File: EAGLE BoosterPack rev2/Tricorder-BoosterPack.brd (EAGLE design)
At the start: 63.9 x 44.2 mm, 39 parts, among them U1 MAG3110, U2 LMT70LMT70, U3 HDC1000, U4 OPT3001, U5 LMP91000, U6 PGA900

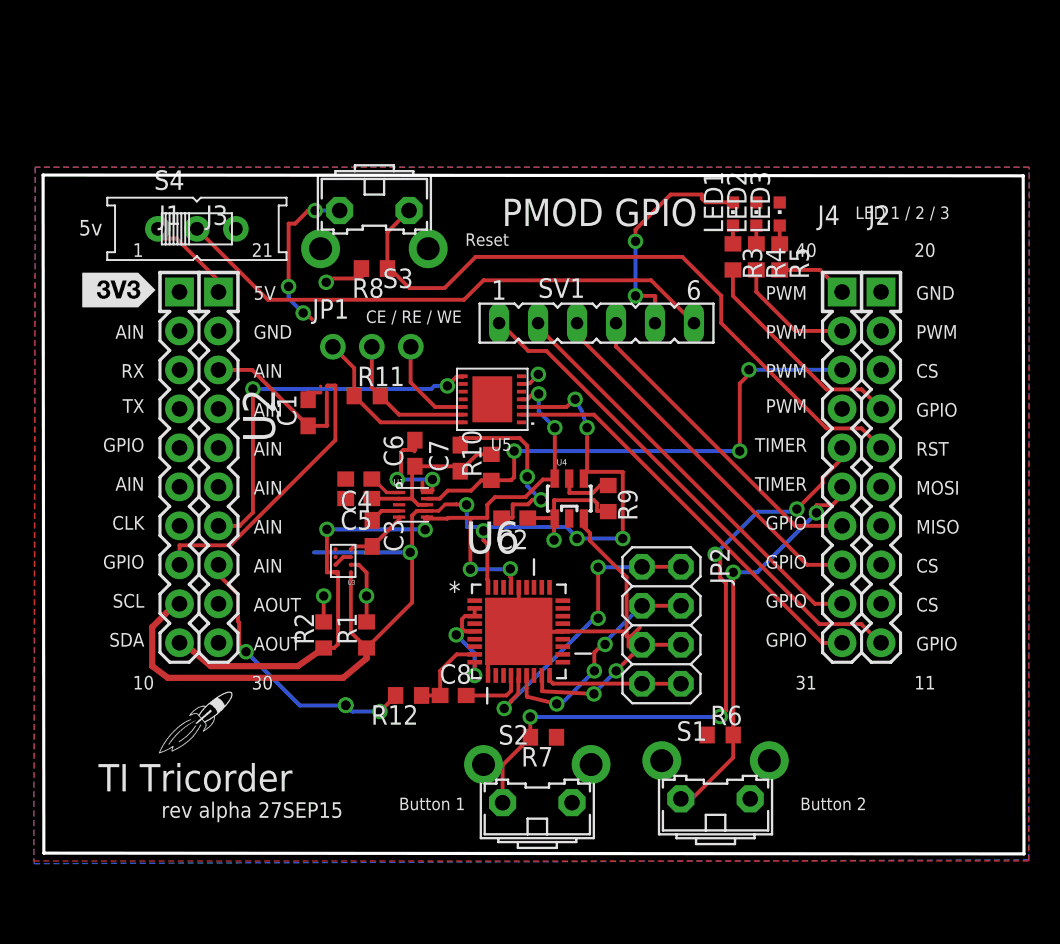
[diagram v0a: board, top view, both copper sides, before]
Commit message: Completed PGA900 circuit, add microSD card reader
Completed PGA900 circuit, add microSD card reader
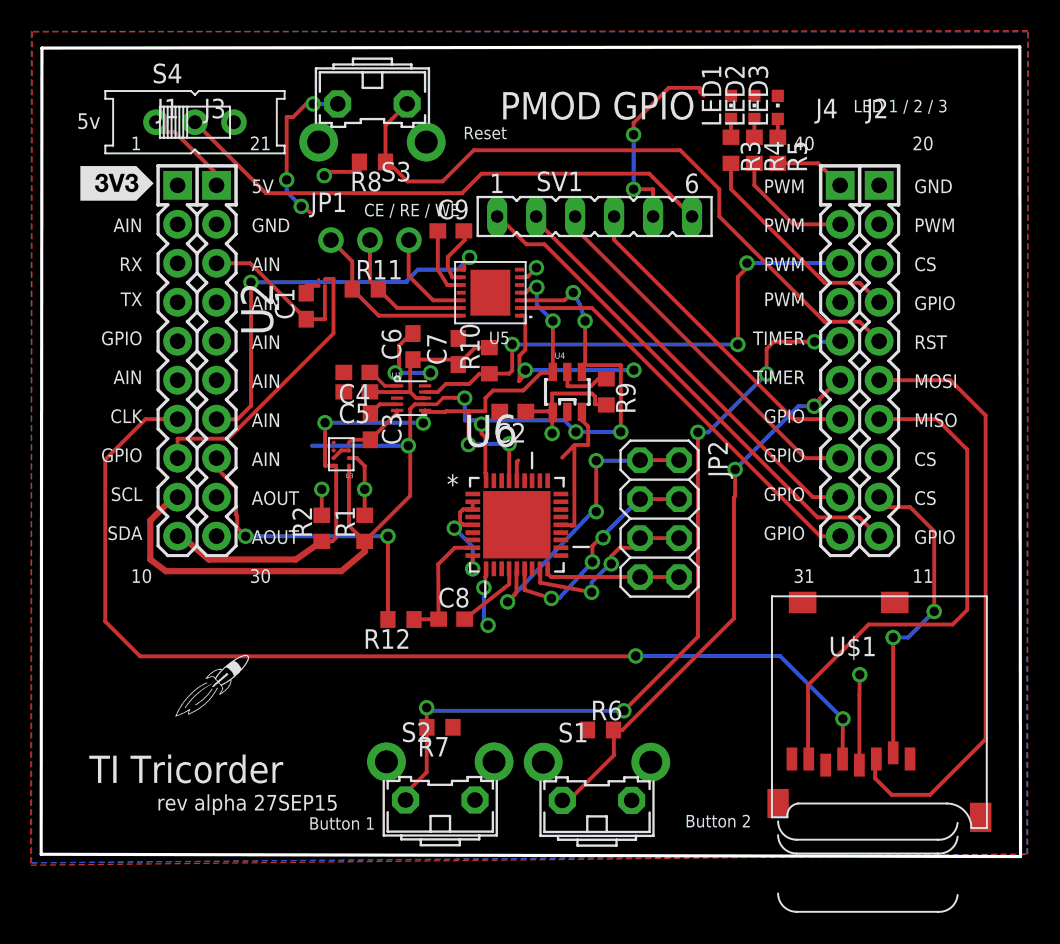
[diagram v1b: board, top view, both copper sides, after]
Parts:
- added C9: 0, adafruit:C0603
- added U$1: MICROSD, adafruit:MICROSD
- moved R6 7.81 mm to (37.9, 8.40)
- moved S1 7.73 mm to (37.7, 5.06)
- moved C6 6.95 mm to (25.7, 33.4)
- moved JP1 6.95 mm to (22.9, 40.3)
- moved LED1 6.95 mm to (46.4, 49.0)
- moved LED2 6.95 mm to (48.0, 49.0)
- moved LED3 6.95 mm to (49.5, 49.0)
- moved R10 6.95 mm to (30.7, 32.5)
- moved S3 6.95 mm to (23.1, 48.0)
- moved S4 6.95 mm to (11.5, 48.0)
- moved SV1 6.95 mm to (37.5, 41.9)
- moved U2 6.95 mm to (19.8, 37.5)
- moved JP2 6.95 mm to (41.8, 22.2)
- moved A1 6.95 mm to (10.4, 33.7)
- moved C1 6.95 mm to (18.7, 36.0)
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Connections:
- new net N$13: C9.2, U5.9
- new net N$7: C9.1, U5.10
- net 3V: now also U$1.4
- net GND: now also U$1.6, U$1.CD1, U$1.CD2, U$1.MT1, U$1.MT2
- net MISO: now also U$1.7
- net MOSI: now also U$1.3
- net SCLK: now also U$1.5
- net SD_CS: now also U$1.2
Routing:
- net SCLK: track 0.00 -> 69.7 mm, vias 0 -> 2
- net MOSI: track 0.00 -> 39.4 mm
- net MISO: track 0.00 -> 34.3 mm
- net SD_CS: track 0.00 -> 21.0 mm, vias 0 -> 2
- net GND: track 77.8 -> 65.3 mm, vias 9 -> 11
- net BTN1: track 41.5 -> 52.5 mm, vias 4 -> 5
- net BTN0: track 26.6 -> 36.2 mm
- net 3V: track 27.2 -> 33.1 mm, vias 7 -> 8
- net N$7: track 0.00 -> 4.60 mm
- net N$13: track 0.00 -> 4.28 mm
- net N$12: track 5.50 -> 7.88 mm
- net PGA900_VOUT: track 18.5 -> 20.6 mm, vias 4 -> 2
- net LMP91000_VOUT: track 24.7 -> 26.8 mm
- net N$10: track 4.06 -> 4.69 mm
- net VINPN: track 12.0 -> 12.5 mm
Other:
- board size 63.9 x 44.2 mm -> 63.8 x 52.8 mm

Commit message: Hardware Design Lock
Short of finding any showstopper bugs, the hardware design and BOM is
locked.
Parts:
- C1: value (none) -> 0
- moved C5 2.83 mm to (22.3, 33.2), turned to 90 degrees
- moved C6 1.95 mm to (23.8, 33.3)
- moved U$2 1.43 mm to (13.8, 10.5)
- moved C4 1.31 mm to (21.1, 30.8)
- moved C3 1.27 mm to (22.4, 29.3), turned to 180 degrees
- renumbered U$1 to U7
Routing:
- net GND: track 65.3 -> 102.8 mm, vias 11 -> 17
- net SCL: track 78.4 -> 71.5 mm, vias 7 -> 6
- net PGA900_VOUT: track 20.6 -> 17.9 mm
- net N$11: track 11.5 -> 12.7 mm
- net N$9: track 2.14 -> 2.73 mm
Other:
- board text added: "LED 1/2/PWR"
- board text removed: "LED 1 / 2 / 3"

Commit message: MAG3110 Circuit Fix
Removed R10, renumbered components
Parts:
- removed R12: 10k, resistor:R0603
- R10: value 10k -> 0
- R11: value 0 -> 10k
- moved R11 21.7 mm to (24.9, 15.6), turned to 180 degrees
- moved R10 9.33 mm to (22.6, 37.1), turned to 0 degrees
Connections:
- removed net N$11: C5.1, C6.1, C7.1, R10.2, U1.2, U1.8
- net 3V: now also C5.1, C6.1, C7.1, U1.2, U1.8
- net CE: now also R10.1; no longer R11.1
- net MAG_INT: no longer R10.1
- net N$12: now also R11.1; no longer R12.1
- net PGA900_VOUT: now also R11.2; no longer R12.2
- net RE: now also R10.2; no longer R11.2
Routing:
- net 3V: track 33.1 -> 46.0 mm, vias 8 -> 9
- net N$11: track 12.7 -> 0.00 mm
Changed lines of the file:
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@@
 <element name="C6" library="adafruit" package="C0603" value="1u" x="23.755" y="33.286" rot="R90"/>
 <element name="C7" library="adafruit" package="C0603" value="100n" x="28.657" y="33.065" rot="R90"/>
-<element name="R10" library="resistor" package="R0603" value="10k" x="30.685" y="32.465" rot="R90"/>
 <element name="U5" library="LMP91000" package="WFDFN-14" value="LMP91000" x="30.75" y="36.9" rot="R90">
 <attribute name="DIGIKEY" value="LMP91000SDE/NOPBCT-ND" x="30.75" y="36.9" size="1.778" layer="27" rot="R90" display="off"/>
 </element>
 <element name="JP1" library="adafruit" package="1X03-CLEANBIG" value="" x="22.9" y="40.325"/>
-<element name="R11" library="resistor" package="R0603" value="0" x="22.6" y="37.125"/>
+<element name="R10" library="resistor" package="R0603" value="0" x="22.6" y="37.125"/>
 <element name="U6" library="PGA900" package="QFN50P600X600X90-37N" value="PGA900" x="32.475" y="21.775">
 <attribute name="PACKAGE" value="QFN-36" x="32.475" y="21.775" size="1.778" layer="27" display="off"/>
@@
 </element>
 <element name="C8" library="adafruit" package="C0603" value="100n" x="28.225" y="15.625"/>
-<element name="R12" library="resistor" package="R0603" value="10k" x="24.925" y="15.6" rot="R180"/>
+<element name="R11" library="resistor" package="R0603" value="10k" x="24.925" y="15.6" rot="R180"/>
 <element name="JP2" library="adafruit" package="2X04" value="" x="41.775" y="22.175" rot="R270"/>
 <element name="C9" library="adafruit" package="C0603" value="0" x="28.175" y="40.925"/>
@@
 <wire x1="54.825" y1="12" x2="54.8" y2="10.65" width="0.254" layer="1"/>
 <via x="54.825" y="12" extent="1-16" drill="0.6096"/>
+<contactref element="U1" pad="8"/>
+<contactref element="C7" pad="1"/>
+<contactref element="C5" pad="1"/>
+<contactref element="C6" pad="1"/>
+<contactref element="U1" pad="2"/>
+<wire x1="22.317" y1="32.399" x2="22.354" y2="32.436" width="0.254" layer="1"/>
+<wire x1="22.354" y1="32.436" x2="23.755" y2="32.436" width="0.254" layer="1"/>
+<wire x1="26.494" y1="30.025" x2="25.8" y2="30.025" width="0.254" layer="1"/>
+<wire x1="25.8" y1="30.025" x2="25.4" y2="30.425" width="0.254" layer="1"/>
+<wire x1="25.4" y1="30.425" x2="24.674" y2="30.425" width="0.254" layer="1"/>
+<wire x1="23.755" y1="32.436" x2="23.966" y2="32.225" width="0.254" layer="1"/>
+<wire x1="23.966" y1="32.225" x2="25.075" y2="32.225" width="0.254" layer="1"/>
+<wire x1="25.075" y1="32.225" x2="25.45" y2="32.2" width="0.254" layer="1"/>
+<wire x1="25.45" y1="32.2" x2="25.4" y2="30.425" width="0.254" layer="1"/>
+<wire x1="28.657" y1="32.215" x2="28.192" y2="32.2" width="0.254" layer="1"/>
+<wire x1="28.192" y1="32.2" x2="26.275" y2="32.2" width="0.254" layer="1"/>
+<wire x1="26.275" y1="32.2" x2="25.45" y2="32.2" width="0.254" layer="1"/>
+<wire x1="26.275" y1="32.2" x2="26.275" y2="34.55" width="0.254" layer="1"/>
+<wire x1="26.275" y1="34.55" x2="26.275" y2="34.9" width="0.254" layer="1"/>
+<via x="26.275" y="34.55" extent="1-16" drill="0.6096"/>
 </signal>
 <signal name="DC">
@@
 <contactref element="A1" pad="38"/>
 <contactref element="U1" pad="9"/>
-<contactref element="R10" pad="1"/>
 <wire x1="46.875" y1="33.525" x2="46.875" y2="37.925" width="0.254" layer="1"/>
 <wire x1="32.175" y1="33.525" x2="46.875" y2="33.525" width="0.254" layer="16"/>
 <wire x1="32.175" y1="31.825" x2="32.175" y2="33.525" width="0.254" layer="1"/>
 <wire x1="31.975" y1="31.625" x2="32.175" y2="31.825" width="0.254" layer="1"/>
-<wire x1="30.775" y1="31.625" x2="31.975" y2="31.625" width="0.254" layer="1"/>
-<wire x1="30.775" y1="31.625" x2="30.685" y2="31.615" width="0.254" layer="1"/>
 <wire x1="47.475" y1="38.525" x2="46.875" y2="37.925" width="0.254" layer="1"/>
 <wire x1="47.475" y1="38.825" x2="47.475" y2="38.525" width="0.254" layer="1"/>
@@
 <wire x1="26.494" y1="30.425" x2="28.475" y2="30.425" width="0.254" layer="1"/>
 <wire x1="28.475" y1="30.425" x2="29.625" y2="31.225" width="0.254" layer="1"/>
-<wire x1="29.625" y1="31.225" x2="29.625" y2="31.6" width="0.254" layer="1"/>
-<wire x1="29.625" y1="31.6" x2="30.04" y2="31.615" width="0.254" layer="1"/>
-<wire x1="30.04" y1="31.615" x2="30.685" y2="31.615" width="0.254" layer="1"/>
+<wire x1="30.075" y1="31.575" x2="29.75" y2="31.25" width="0.254" layer="1"/>
+<wire x1="31.85" y1="31.575" x2="30.075" y2="31.575" width="0.254" layer="1"/>
+<wire x1="29.75" y1="31.25" x2="29.625" y2="31.225" width="0.254" layer="1"/>
+<wire x1="31.85" y1="31.575" x2="31.975" y2="31.625" width="0.254" layer="1"/>
 </signal>
 <signal name="LED1">
@@
 <wire x1="21.971" y1="30.825" x2="21.949" y2="30.803" width="0.254" layer="1"/>
 </signal>
-<signal name="N$11">
-<contactref element="U1" pad="8"/>
-<contactref element="C7" pad="1"/>
-<contactref element="C5" pad="1"/>
-<contactref element="C6" pad="1"/>
-<contactref element="R10" pad="2"/>
-<contactref element="U1" pad="2"/>
-<wire x1="30.675" y1="33.325" x2="30.685" y2="33.315" width="0.254" layer="1"/>
-<wire x1="30.675" y1="33.325" x2="29.565" y2="32.215" width="0.254" layer="1"/>
-<wire x1="29.565" y1="32.215" x2="28.657" y2="32.215" width="0.254" layer="1"/>
-<wire x1="22.317" y1="32.399" x2="22.354" y2="32.436" width="0.254" layer="1"/>
-<wire x1="22.354" y1="32.436" x2="23.755" y2="32.436" width="0.254" layer="1"/>
-<wire x1="26.494" y1="30.025" x2="25.8" y2="30.025" width="0.254" layer="1"/>
-<wire x1="25.8" y1="30.025" x2="25.4" y2="30.425" width="0.254" layer="1"/>
-<wire x1="25.4" y1="30.425" x2="24.674" y2="30.425" width="0.254" layer="1"/>
-<wire x1="23.755" y1="32.436" x2="23.966" y2="32.225" width="0.254" layer="1"/>
-<wire x1="23.966" y1="32.225" x2="25.075" y2="32.225" width="0.254" layer="1"/>
-<wire x1="25.075" y1="32.225" x2="25.45" y2="32.2" width="0.254" layer="1"/>
-<wire x1="25.45" y1="32.2" x2="25.4" y2="30.425" width="0.254" layer="1"/>
-<wire x1="28.657" y1="32.215" x2="28.192" y2="32.2" width="0.254" layer="1"/>
-<wire x1="28.192" y1="32.2" x2="25.45" y2="32.2" width="0.254" layer="1"/>
-</signal>
 <signal name="VREF">
 <contactref element="U5" pad="11"/>
@@
 <contactref element="U5" pad="14"/>
 <contactref element="JP1" pad="1"/>
-<contactref element="R11" pad="1"/>
+<contactref element="R10" pad="1"/>
 <wire x1="28.85" y1="35.4" x2="23.475" y2="35.4" width="0.254" layer="1"/>
 <wire x1="23.475" y1="35.4" x2="21.75" y2="37.125" width="0.254" layer="1"/>
@@
 <contactref element="U5" pad="13"/>
 <contactref element="JP1" pad="2"/>
-<contactref element="R11" pad="2"/>
+<contactref element="R10" pad="2"/>
 <wire x1="22.9" y1="40.325" x2="22.9" y2="37.675" width="0.254" layer="1"/>
 <wire x1="22.9" y1="37.675" x2="23.45" y2="37.125" width="0.254" layer="1"/>
@@
 <contactref element="U6" pad="8"/>
 <contactref element="C8" pad="1"/>
-<contactref element="R12" pad="1"/>
+<contactref element="R11" pad="1"/>
 <wire x1="29.6048" y1="20.2764" x2="28.4264" y2="20.2764" width="0.254" layer="1"/>
 <wire x1="28.4264" y1="20.2764" x2="27.35" y2="19.2" width="0.254" layer="1"/>
@@
 <signal name="PGA900_VOUT">
 <contactref element="A1" pad="28"/>
-<contactref element="R12" pad="2"/>
+<contactref element="R11" pad="2"/>
 <wire x1="22.075" y1="15.6" x2="24.075" y2="15.6" width="0.254" layer="1"/>
 <wire x1="17.1" y1="26.125" x2="22.075" y2="15.6" width="0.254" layer="16"/>

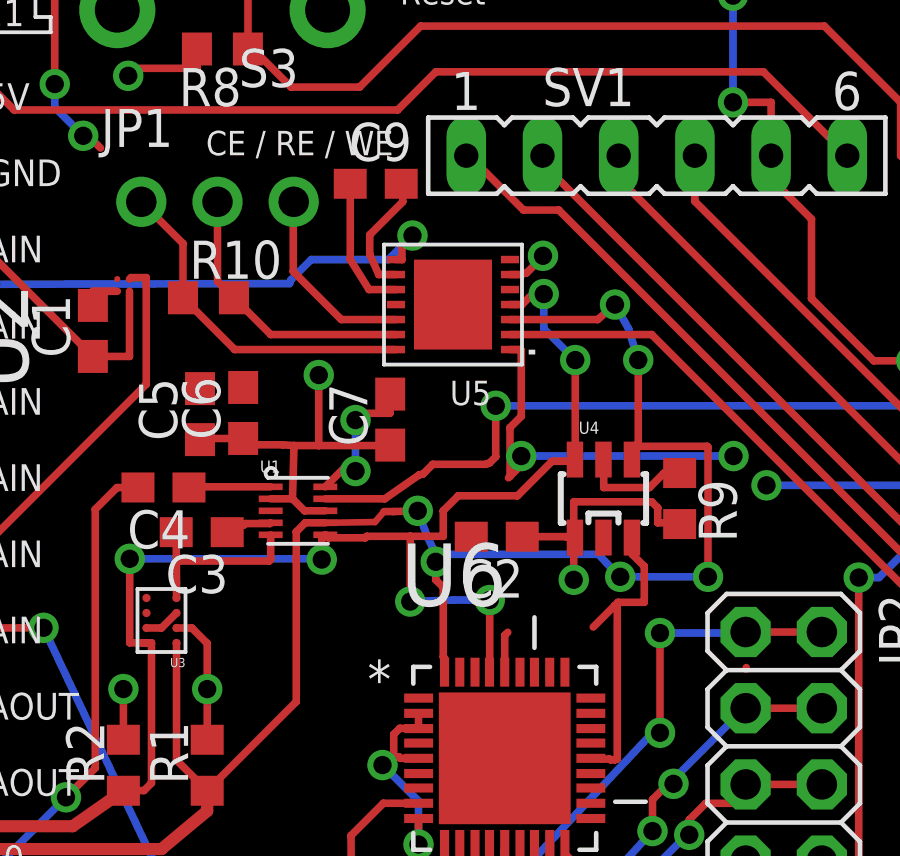
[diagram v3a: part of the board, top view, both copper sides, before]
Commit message: Revised BOM
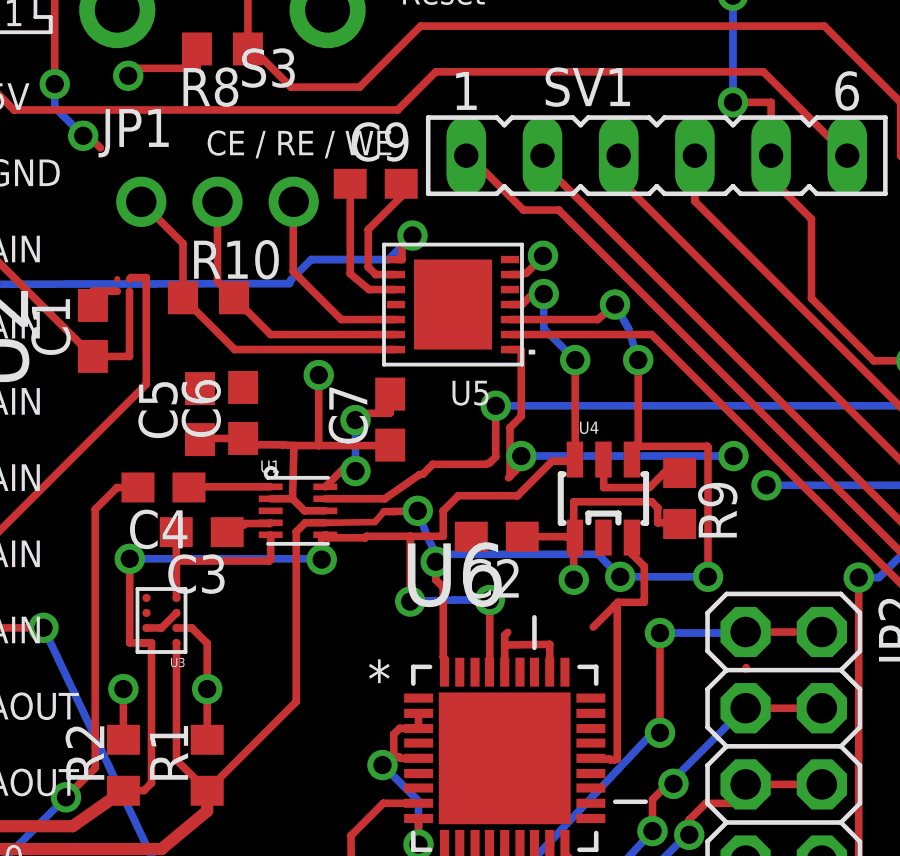
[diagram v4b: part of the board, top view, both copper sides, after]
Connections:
- net GND: now also U6.29
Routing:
- net GND: track 102.8 -> 105.3 mm
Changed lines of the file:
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@@
 <element name="C7" library="adafruit" package="C0603" value="100n" x="28.657" y="33.065" rot="R90"/>
 <element name="U5" library="LMP91000" package="WFDFN-14" value="LMP91000" x="30.75" y="36.9" rot="R90">
-<attribute name="DIGIKEY" value="LMP91000SDE/NOPBCT-ND" x="30.75" y="36.9" size="1.778" layer="27" rot="R90" display="off"/>
+<attribute name="DIGIKEY" value="LMP91000" x="30.75" y="36.9" size="1.778" layer="27" rot="R90" display="off"/>
 </element>
 <element name="JP1" library="adafruit" package="1X03-CLEANBIG" value="" x="22.9" y="40.325"/>
@@
 <wire x1="36.725" y1="29.125" x2="36.725" y2="28.575" width="0.254" layer="1"/>
 <wire x1="36.725" y1="29.125" x2="36.715" y2="29.1329" width="0.254" layer="1"/>
-<wire x1="32.475" y1="24.6452" x2="32.475" y2="25.875" width="0.254" layer="1"/>
+<wire x1="32.475" y1="24.6452" x2="32.475" y2="25.55" width="0.254" layer="1"/>
+<wire x1="32.475" y1="25.55" x2="32.475" y2="25.875" width="0.254" layer="1"/>
 <wire x1="32.475" y1="25.875" x2="32.575" y2="25.975" width="0.254" layer="1"/>
 <wire x1="36.15" y1="21.725" x2="36.175" y2="21.75" width="0.254" layer="1"/>
@@
 <wire x1="24.625" y1="28.35" x2="21.5511" y2="28.35" width="0.254" layer="1"/>
 <wire x1="21.5511" y1="28.35" x2="21.52900625" y2="28.37209375" width="0.254" layer="1"/>
+<contactref element="U6" pad="29"/>
+<wire x1="33.9736" y1="24.6452" x2="33.975" y2="25.575" width="0.254" layer="1"/>
+<wire x1="33.975" y1="25.575" x2="32.475" y2="25.55" width="0.254" layer="1"/>
 </signal>
 <signal name="N$1">
@@
 <contactref element="U5" pad="10"/>
 <wire x1="28.85" y1="37.4" x2="27.95" y2="37.4" width="0.254" layer="1"/>
-<wire x1="27.95" y1="37.4" x2="27.325" y2="38.4" width="0.254" layer="1"/>
-<wire x1="27.325" y1="38.4" x2="27.325" y2="40.925" width="0.254" layer="1"/>
-</signal>
-<signal name="N$13">
+<wire x1="27.95" y1="37.4" x2="27.325" y2="37.925" width="0.254" layer="1"/>
+<wire x1="27.325" y1="37.925" x2="27.325" y2="40.925" width="0.254" layer="1"/>
+</signal>
+<signal name="N$11">
 <contactref element="U5" pad="9"/>
 <contactref element="C9" pad="2"/>
-<wire x1="28.85" y1="37.9" x2="28.275" y2="37.9" width="0.254" layer="1"/>
-<wire x1="28.275" y1="37.9" x2="27.975" y2="38.575" width="0.254" layer="1"/>
-<wire x1="27.975" y1="38.575" x2="27.975" y2="39.225" width="0.254" layer="1"/>
-<wire x1="28.925" y1="40.825" x2="29.025" y2="40.925" width="0.254" layer="1"/>
-<wire x1="27.975" y1="39.225" x2="29.075" y2="40.325" width="0.254" layer="1"/>
-<wire x1="29.075" y1="40.325" x2="29.075" y2="40.875" width="0.254" layer="1"/>
-<wire x1="29.075" y1="40.875" x2="29.025" y2="40.925" width="0.254" layer="1"/>
+<wire x1="29.025" y1="40.925" x2="29.025" y2="40.5" width="0.254" layer="1"/>
+<wire x1="29.025" y1="40.5" x2="27.925" y2="39.4" width="0.254" layer="1"/>
+<wire x1="27.925" y1="39.4" x2="27.925" y2="38.15" width="0.254" layer="1"/>
+<wire x1="27.925" y1="38.15" x2="28.175" y2="37.9" width="0.254" layer="1"/>
+<wire x1="28.175" y1="37.9" x2="28.85" y2="37.9" width="0.254" layer="1"/>
 </signal>
 </signals>
